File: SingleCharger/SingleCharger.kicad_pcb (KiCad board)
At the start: 2 copper layers, 120 x 130 mm, 94 parts, among them J1 Bus_PCI_Express_x1, J2 Conn_01x03_Pin, J3 Conn_01x02_Pin, J4 Conn_01x02_Pin, J5 Conn_01x03_Pin, Q2 TPHR8504PL,LQ(M1W, Q5 NMOS, Q6 NMOS, Q7 NMOS, Q8 NMOS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

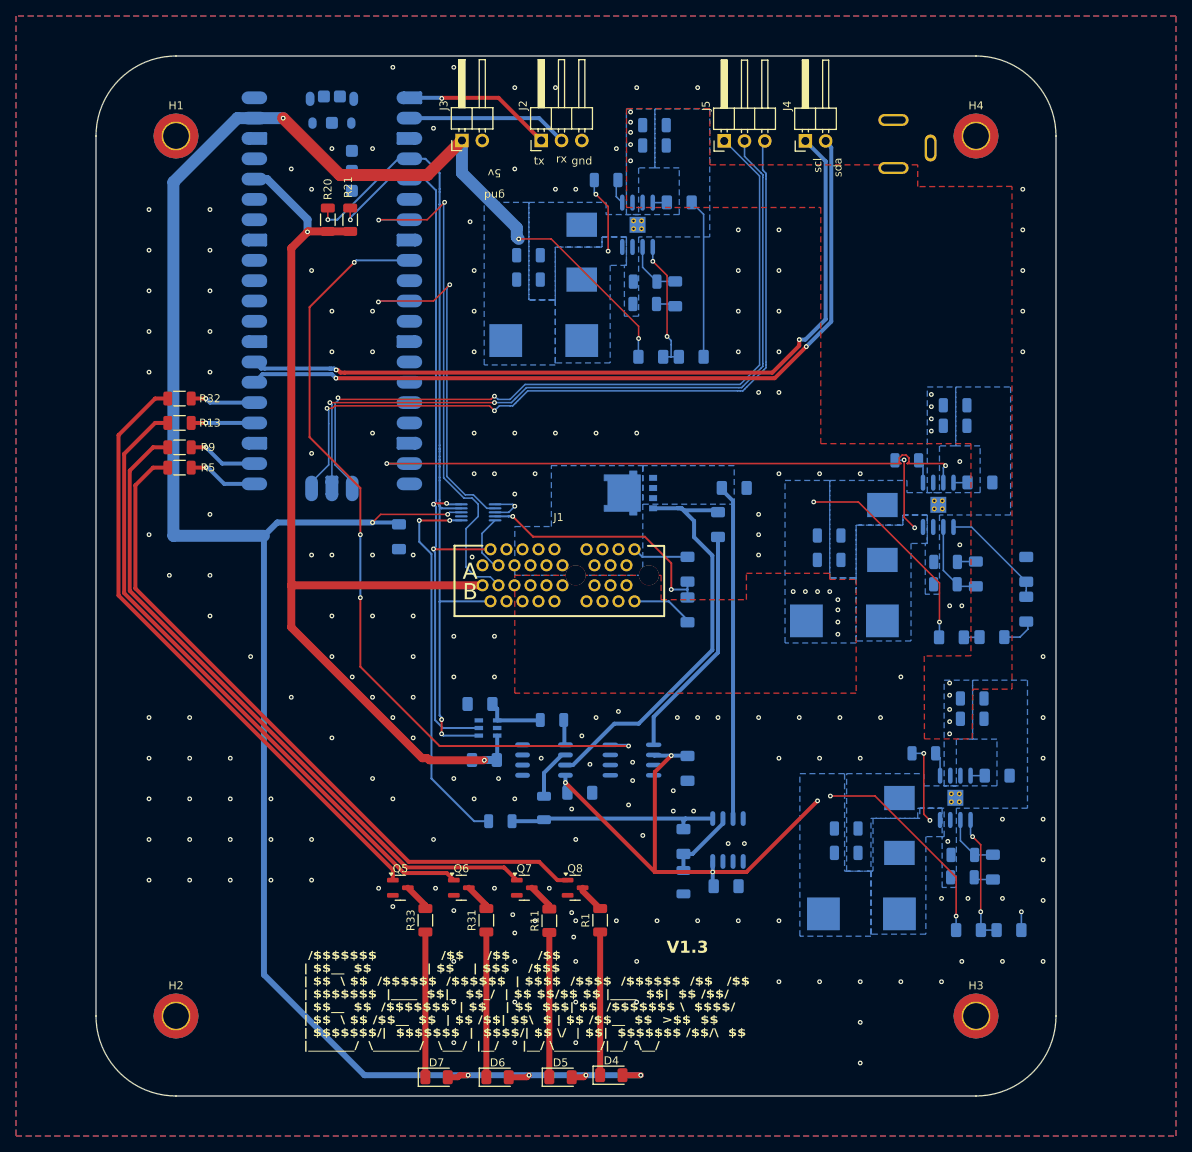
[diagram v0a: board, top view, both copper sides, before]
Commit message: Fixed some issues for hopeful stability in analog measuremnets.
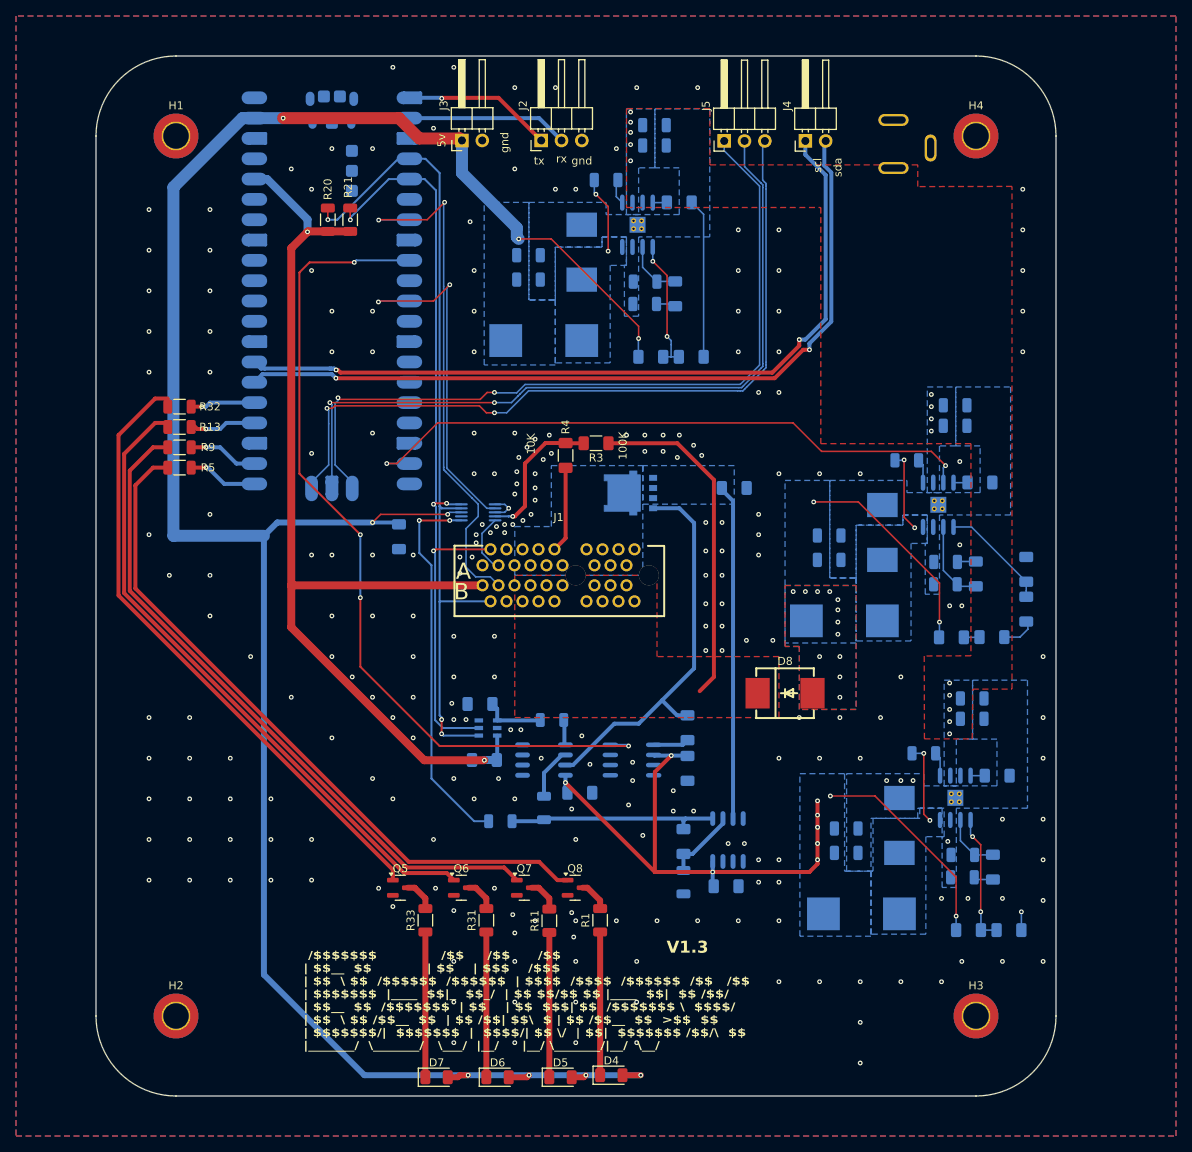
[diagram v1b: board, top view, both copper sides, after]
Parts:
- added D8: B560C-13-F, COMPONENTS:SMC_L7.1-W6.2-LS8.1-RD, F.Cu at (151.1, 104.6)
- R3, R4: moved to F.Cu
- moved R10 25.7 mm to (138.9, 109.0)
- moved R3 23.8 mm to (127.5, 73.4), turned to 180 degrees
- moved R4 20.8 mm to (123.7, 74.9), turned to -90 degrees
- moved R32 1.02 mm to (75.4, 68.8)
- moved R13 0.51 mm to (75.4, 71.4)
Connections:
- J1 pad B10: +24V -> /BatteryCC/B+
- J1 pad B11: +24V -> /BatteryCC/B+
- J1 pad B12: +24V -> /BatteryCC/B+
- J1 pad B13: +24V -> /BatteryCC/B+
- J1 pad B14: +24V -> /BatteryCC/B+
- J1 pad B15: +24V -> /BatteryCC/B+
- J1 pad B16: +24V -> /BatteryCC/B+
- J1 pad B17: +24V -> /BatteryCC/B+
- J1 pad B18: +24V -> /BatteryCC/B+
- J1 pad B6: +24V -> /BatteryCC/B+
- J1 pad B7: +24V -> /BatteryCC/B+
- J1 pad B8: +24V -> /BatteryCC/B+
- J1 pad B9: +24V -> /BatteryCC/B+
- R3 pad 1: +24V -> /BatteryCC/B+
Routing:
- net /BatteryCC/B+: track 0.00 -> 42.2 mm
- net Net-(U8-OUTB): track 29.3 -> 4.47 mm
- net Net-(U1-AIN0): track 31.8 -> 18.0 mm, vias 2 -> 1
- net +24V: track 34.4 -> 26.5 mm, vias 10 -> 14
- net +12V: track 91.5 -> 96.1 mm, vias 6 -> 10
- net /BatteryCC/ChargeLV: track 102.5 -> 106.8 mm
- net +5V: track 286.2 -> 282.3 mm
- net /BatteryCC/Charge: track 53.0 -> 49.1 mm
- net /BatteryCC/B-: track 6.98 -> 10.8 mm
- net /Power Delivery/EN_BAT_V: track 77.3 -> 79.2 mm
- net GND: track 27.5 -> 26.0 mm, vias 202 -> 249
- net Net-(U2-GP18): track 7.90 -> 8.53 mm
- net /BatteryCC/ALERT/RDY: track 45.5 -> 44.9 mm
- net /BatteryCC/Battery/EEPROM_WC: track 66.7 -> 66.1 mm
- added copper zone on F.Cu, net /BatteryCC/B+
- added copper zone on In1.Cu, net GND
- added copper zone on In2.Cu, net GND
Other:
- copper layers 2 -> 4

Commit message: Fixed silkscreen.
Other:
- board text added: "V1.4"
- board text removed: "V1.3"
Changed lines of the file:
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@@
 		)
 	)
-	(gr_text "V1.3"
+	(gr_text "V1.4"
 		(at 138.938 136.398 0)
 		(layer "F.SilkS" knockout)
@@
 			)
 		)
-		(render_cache "V1.3" 0
+		(render_cache "V1.4" 0
 			(polygon
 				(pts
@@
 			(polygon
 				(pts
-					(xy 140.707631 136.057053) (xy 140.735841 136.05916) (xy 140.755716 136.05916) (xy 140.805245 136.053674)
-					(xy 140.846328 136.038085) (xy 140.88083 136.012631) (xy 140.90724 135.978927) (xy 140.923234 135.939249)
-					(xy 140.928823 135.891823) (xy 140.923549 135.845703) (xy 140.908542 135.807491) (xy 140.883944 135.775411)
-					(xy 140.851631 135.750963) (xy 140.813566 135.7361) (xy 140.768081 135.730897) (xy 140.720332 135.736799)
-					(xy 140.680631 135.753696) (xy 140.647089 135.78173) (xy 140.622057 135.818) (xy 140.606638 135.861129)
-					(xy 140.601202 135.91298) (xy 140.220733 135.91298) (xy 140.244145 135.793113) (xy 140.282557 135.691147)
-					(xy 140.336828 135.600672) (xy 140.402908 135.52729) (xy 140.481927 135.468906) (xy 140.574641 135.425807)
-					(xy 140.676606 135.399924) (xy 140.792536 135.390911) (xy 140.906286 135.399422) (xy 141.005027 135.423701)
-					(xy 141.094585 135.463882) (xy 141.168426 135.516666) (xy 141.228468 135.583059) (xy 141.273114 135.66257)
-					(xy 141.300372 135.751644) (xy 141.309842 135.853721) (xy 141.304537 135.928895) (xy 141.289809 135.990452)
-					(xy 141.266886 136.040841) (xy 141.215668 136.107764) (xy 141.144246 136.166504) (xy 141.220887 136.198979)
-					(xy 141.283834 136.243929) (xy 141.33503 136.301968) (xy 141.37232 136.370068) (xy 141.395485 136.449346)
-					(xy 141.403632 136.542394) (xy 141.398325 136.619729) (xy 141.382837 136.69081) (xy 141.35747 136.756626)
-					(xy 141.302203 136.846263) (xy 141.228418 136.922497) (xy 141.138989 136.98317) (xy 141.031222 137.029567)
-					(xy 140.913328 137.057644) (xy 140.780538 137.067394) (xy 140.660576 137.059135) (xy 140.551343 137.035123)
-					(xy 140.451176 136.995953) (xy 140.360811 136.939767) (xy 140.282826 136.864923) (xy 140.216245 136.769082)
-					(xy 140.182616 136.698693) (xy 140.162847 136.630413) (xy 140.152621 136.560644) (xy 140.1492 136.489638)
-					(xy 140.559528 136.489638) (xy 140.567053 136.561161) (xy 140.587699 136.616041) (xy 140.620253 136.658165)
-					(xy 140.663912 136.689345) (xy 140.717488 136.708759) (xy 140.783743 136.715684) (xy 140.853882 136.70826)
-					(xy 140.905392 136.688247) (xy 140.942929 136.657158) (xy 140.970617 136.615644) (xy 140.98745 136.568026)
-					(xy 140.993304 136.512627) (xy 140.985884 136.446921) (xy 140.965436 136.396507) (xy 140.932853 136.357747)
-					(xy 140.890109 136.328698) (xy 140.842634 136.311316) (xy 140.788964 136.305356) (xy 140.749305 136.308471)
-					(xy 140.707631 136.315798)
+					(xy 141.257086 136.375698) (xy 141.444664 136.375698) (xy 141.444664 136.692237) (xy 141.257086 136.692237)
+					(xy 141.257086 137.017569) (xy 140.876067 137.017569) (xy 140.876067 136.692237) (xy 140.108168 136.692237)
+					(xy 140.108168 136.426348) (xy 140.139112 136.375698) (xy 140.511077 136.375698) (xy 140.876067 136.375698)
+					(xy 140.876067 135.751414) (xy 140.511077 136.375698) (xy 140.139112 136.375698) (xy 140.715691 135.431944)
+					(xy 141.257086 135.431944)
 				)
 			)
